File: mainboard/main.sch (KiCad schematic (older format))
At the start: 38 parts, among them Q1 TIP120, U1 LevelShifter

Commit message: first prototype
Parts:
- removed C1: 1uF, Capacitor_THT:CP_Radial_D5.0mm_P2.50mm, symbol Device:CP
- removed CellVoltageOpAmp1: LM358, Package_DIP:DIP-8_W7.62mm_Socket, symbol Amplifier_Operational:LM358
- removed R_Cell1_Vdiv_A1: 33K, Resistor_THT:R_Axial_DIN0207_L6.3mm_D2.5mm_P7.62mm_Horizontal, symbol Device:R
- removed R_Cell1_Vdiv_B1: 100K, Resistor_THT:R_Axial_DIN0207_L6.3mm_D2.5mm_P2.54mm_Vertical, symbol Device:R
- removed R_V_Cell2_1, R_V_Cell2_2, R_V_Cell3_2: 47K, Resistor_THT:R_Axial_DIN0207_L6.3mm_D2.5mm_P2.54mm_Vertical, symbol Device:R
- removed R_V_Cell2_3, R_V_Cell2_4, R_V_Cell3_3, R_V_Cell3_4: 33K, Resistor_THT:R_Axial_DIN0207_L6.3mm_D2.5mm_P2.54mm_Vertical, symbol Device:R
- removed R_V_Cell3_1: 47K, Resistor_THT:R_Axial_DIN0207_L6.3mm_D2.5mm_P5.08mm_Vertical, symbol Device:R
- added Diode2, Diode3: D, Diode_THT:D_T-1_P5.08mm_Horizontal, symbol Device:D
- added RV2: R_POT3Bat, Potentiometer_THT:Potentiometer_Bourns_3296W_Vertical, symbol Device:R_POT_TRIM
- added RV3: R_POT2, Potentiometer_THT:Potentiometer_Bourns_3296W_Vertical, symbol Device:R_POT_TRIM
- added RV4: R_POT1, Potentiometer_THT:Potentiometer_Bourns_3296W_Vertical, symbol Device:R_POT_TRIM
- renumbered Diode1 to Diode1sw1
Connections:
- net PCheck is gone; now on net P_Check: MicroController1.18 (A7)
- net PowerIN is gone; now on net P_IN: MicroController1.17 (D13/SCK)
- net +3V3: no longer Con_Switch1.3 (Pin_3)
- net +BATT: now also RV3.3
- net BATT_Cell_1_2: now also Diode3.2 (A)
- net BATT_Cell_2_3: now also Diode2.2 (A)
- net GND: now also Con_Switch1.3 (Pin_3), RV2.1, RV3.1, RV4.1
- net op2: now also RV2.2
- net op3: now also RV3.2
- net op4: now also RV4.2
- new net: Diode2.1 (K), RV2.3
- new net: Diode3.1 (K), RV4.3

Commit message: again
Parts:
- added R1: ?, Resistor_THT:R_Axial_DIN0207_L6.3mm_D2.5mm_P2.54mm_Vertical, symbol Device:R
- MicroController1: footprint CustomFootprints:Arduino_Pro_Mini_Socket_IZOKEE -> CustomFootprints:Arduino_Pro_Mini_Socket_IZOKEE_no_programming
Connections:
- net at Diode1sw1.1 (K), RV1.3, R_T1.1: now also R1.2; no longer Switch_Connector1.2 (Pin_2)
- new net: R1.1, Switch_Connector1.2 (Pin_2)
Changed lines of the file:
@@
 F 0 "MicroController1" H 2200 2765 50  0000 C CNN
 F 1 "IZOKEEProMini" H 2200 2674 50  0000 C CNN
-F 2 "CustomFootprints:Arduino_Pro_Mini_Socket_IZOKEE" H 2200 800 50  0001 C CNN
+F 2 "CustomFootprints:Arduino_Pro_Mini_Socket_IZOKEE_no_programming" H 2200 800 50  0001 C CNN
 F 3 "" H 2200 800 50  0001 C CNN
 	1    2300 1700
@@
 	-1   0    0    1
 $EndComp
-Connection ~ 5400 1000
 Wire Wire Line
 	5100 1000 5400 1000
-$Comp
-L Transistor_BJT:TIP120 Q1
-U 1 1 5E39FC69
-P 5900 1000
-F 0 "Q1" H 6107 1046 50  0000 L CNN
-F 1 "TIP120" H 6107 955 50  0000 L CNN
-F 2 "Package_TO_SOT_THT:TO-220-3_Vertical" H 6100 925 50  0001 L CIN
-F 3 "http://www.fairchildsemi.com/ds/TI/TIP120.pdf" H 5900 1000 50  0001 L CNN
-	1    5900 1000
-	1    0    0    -1
-$EndComp
 $Comp
 L Device:D Diode1sw1
@@
 F 3 "~" H 5400 850 50  0001 C CNN
 	1    5400 850
-	0    -1   -1   0
-$EndComp
-$Comp
-L Device:R R_T1
-U 1 1 5E3B3275
-P 5550 1000
-F 0 "R_T1" H 5620 1046 50  0000 L CNN
-F 1 "1K" H 5620 955 50  0000 L CNN
-F 2 "Resistor_THT:R_Axial_DIN0207_L6.3mm_D2.5mm_P5.08mm_Vertical" V 5480 1000 50  0001 C CNN
-F 3 "~" H 5550 1000 50  0001 C CNN
-	1    5550 1000
 	0    -1   -1   0
 $EndComp
@@
 Wire Wire Line
 	4300 700  4300 800
-Wire Wire Line
-	4300 900  5100 900
 Wire Wire Line
 	5550 1500 5550 1300
@@
 $EndComp
 $Comp
-L power:GND #PWR?
+L power:GND #PWR0126
 U 1 1 5E5F3BCE
 P 3850 1850
-F 0 "#PWR?" H 3850 1600 50  0001 C CNN
+F 0 "#PWR0126" H 3850 1600 50  0001 C CNN
 F 1 "GND" V 3855 1722 50  0000 R CNN
 F 2 "" H 3850 1850 50  0001 C CNN
@@
 	0    1    -1   0
 $EndComp
+Connection ~ 5400 1000
+$Comp
+L Device:R R_T1
+U 1 1 5E3B3275
+P 5550 1000
+F 0 "R_T1" H 5620 1046 50  0000 L CNN
+F 1 "1K" H 5620 955 50  0000 L CNN
+F 2 "Resistor_THT:R_Axial_DIN0207_L6.3mm_D2.5mm_P5.08mm_Vertical" V 5480 1000 50  0001 C CNN
+F 3 "~" H 5550 1000 50  0001 C CNN
+	1    5550 1000
+	0    -1   -1   0
+$EndComp
+$Comp
+L Transistor_BJT:TIP120 Q1
+U 1 1 5E39FC69
+P 5900 1000
+F 0 "Q1" H 6107 1046 50  0000 L CNN
+F 1 "TIP120" H 6107 955 50  0000 L CNN
+F 2 "Package_TO_SOT_THT:TO-220-3_Vertical" H 6100 925 50  0001 L CIN
+F 3 "http://www.fairchildsemi.com/ds/TI/TIP120.pdf" H 5900 1000 50  0001 L CNN
+	1    5900 1000
+	1    0    0    -1
+$EndComp
+$Comp
+L Device:R R1
+U 1 1 5E5F87D4
+P 4800 900
+F 0 "R1" H 4870 946 50  0000 L CNN
+F 1 "?" H 4870 855 50  0000 L CNN
+F 2 "Resistor_THT:R_Axial_DIN0207_L6.3mm_D2.5mm_P2.54mm_Vertical" V 4730 900 50  0001 C CNN
+F 3 "~" H 4800 900 50  0001 C CNN
+	1    4800 900
+	0    -1   -1   0
+$EndComp
+Wire Wire Line
+	4950 900  5100 900
+Wire Wire Line
+	4650 900  4300 900
 $EndSCHEMATC

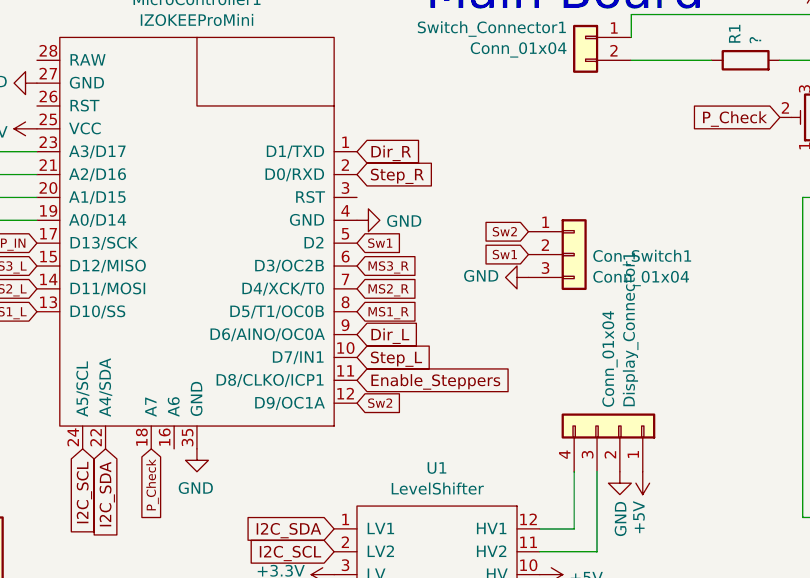
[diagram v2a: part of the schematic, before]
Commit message: pwm pins
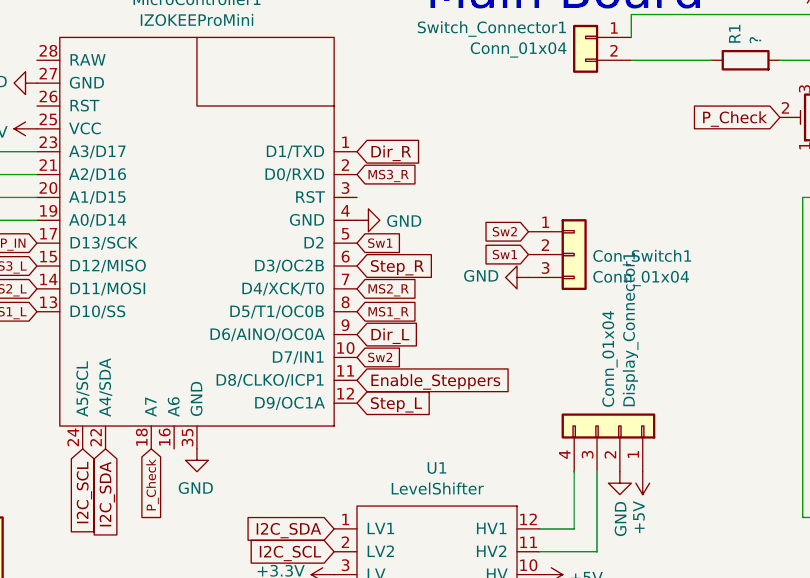
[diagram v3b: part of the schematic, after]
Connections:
- net MS3_R: now also MicroController1.2 (D0/RXD); no longer MicroController1.6 (D3/OC2B)
- net Step_L: now also MicroController1.12 (D9/OC1A); no longer MicroController1.10 (D7/IN1)
- net Step_R: now also MicroController1.6 (D3/OC2B); no longer MicroController1.2 (D0/RXD)
- net Sw2: now also MicroController1.10 (D7/IN1); no longer MicroController1.12 (D9/OC1A)
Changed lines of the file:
@@
 	1    0    0    -1
 $EndComp
-Text GLabel 3100 1800 2    40   Input ~ 0
+Text GLabel 3100 1400 2    40   Input ~ 0
 MS3_R
 Text GLabel 3100 1900 2    40   Input ~ 0
@@
 Text GLabel 3100 1300 2    50   Input ~ 0
 Dir_R
-Text GLabel 3100 1400 2    50   Input ~ 0
+Text GLabel 3100 1800 2    50   Input ~ 0
 Step_R
 Text GLabel 3100 2100 2    50   Input ~ 0
 Dir_L
-Text GLabel 3100 2200 2    50   Input ~ 0
+Text GLabel 3100 2400 2    50   Input ~ 0
 Step_L
 Text GLabel 1800 6550 0    50   Input ~ 0
@@
 Text GLabel 3100 1700 2    40   Input ~ 0
 Sw1
-Text GLabel 3100 2400 2    40   Input ~ 0
+Text GLabel 3100 2200 2    40   Input ~ 0
 Sw2
 Text GLabel 3850 1750 0    40   Input ~ 0

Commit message: larger capacitor footprints
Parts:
- C2, C_MD_L1, C_MD_L2: footprint Capacitor_THT:CP_Radial_D5.0mm_P2.50mm -> Capacitor_THT:CP_Radial_D6.3mm_P2.50mm
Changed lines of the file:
@@
 F 0 "C_MD_L2" H 1168 7146 50  0000 L CNN
 F 1 "100uF" H 1168 7055 50  0000 L CNN
-F 2 "Capacitor_THT:CP_Radial_D5.0mm_P2.50mm" H 1088 6950 50  0001 C CNN
+F 2 "Capacitor_THT:CP_Radial_D6.3mm_P2.50mm" H 1088 6950 50  0001 C CNN
 F 3 "~" H 1050 7100 50  0001 C CNN
 	1    1050 7100
@@
 F 0 "C_MD_L1" H 1118 4896 50  0000 L CNN
 F 1 "100uF" H 1118 4805 50  0000 L CNN
-F 2 "Capacitor_THT:CP_Radial_D5.0mm_P2.50mm" H 1038 4700 50  0001 C CNN
+F 2 "Capacitor_THT:CP_Radial_D6.3mm_P2.50mm" H 1038 4700 50  0001 C CNN
 F 3 "~" H 1000 4850 50  0001 C CNN
 	1    1000 4850
@@
 F 0 "C2" H 10068 2246 50  0000 L CNN
 F 1 "1uF" H 10068 2155 50  0000 L CNN
-F 2 "Capacitor_THT:CP_Radial_D5.0mm_P2.50mm" H 9988 2050 50  0001 C CNN
+F 2 "Capacitor_THT:CP_Radial_D6.3mm_P2.50mm" H 9988 2050 50  0001 C CNN
 F 3 "~" H 9950 2200 50  0001 C CNN
 	1    9950 2200

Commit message: Mainboard changes
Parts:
- C2, C_MD_L1, C_MD_L2: footprint Capacitor_THT:CP_Radial_D6.3mm_P2.50mm -> Capacitor_THT:CP_Radial_D5.0mm_P2.50mm
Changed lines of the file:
@@
 F 0 "C_MD_L2" H 1168 7146 50  0000 L CNN
 F 1 "100uF" H 1168 7055 50  0000 L CNN
-F 2 "Capacitor_THT:CP_Radial_D6.3mm_P2.50mm" H 1088 6950 50  0001 C CNN
+F 2 "Capacitor_THT:CP_Radial_D5.0mm_P2.50mm" H 1088 6950 50  0001 C CNN
 F 3 "~" H 1050 7100 50  0001 C CNN
 	1    1050 7100
@@
 F 0 "C_MD_L1" H 1118 4896 50  0000 L CNN
 F 1 "100uF" H 1118 4805 50  0000 L CNN
-F 2 "Capacitor_THT:CP_Radial_D6.3mm_P2.50mm" H 1038 4700 50  0001 C CNN
+F 2 "Capacitor_THT:CP_Radial_D5.0mm_P2.50mm" H 1038 4700 50  0001 C CNN
 F 3 "~" H 1000 4850 50  0001 C CNN
 	1    1000 4850
@@
 F 0 "C2" H 10068 2246 50  0000 L CNN
 F 1 "1uF" H 10068 2155 50  0000 L CNN
-F 2 "Capacitor_THT:CP_Radial_D6.3mm_P2.50mm" H 9988 2050 50  0001 C CNN
+F 2 "Capacitor_THT:CP_Radial_D5.0mm_P2.50mm" H 9988 2050 50  0001 C CNN
 F 3 "~" H 9950 2200 50  0001 C CNN
 	1    9950 2200

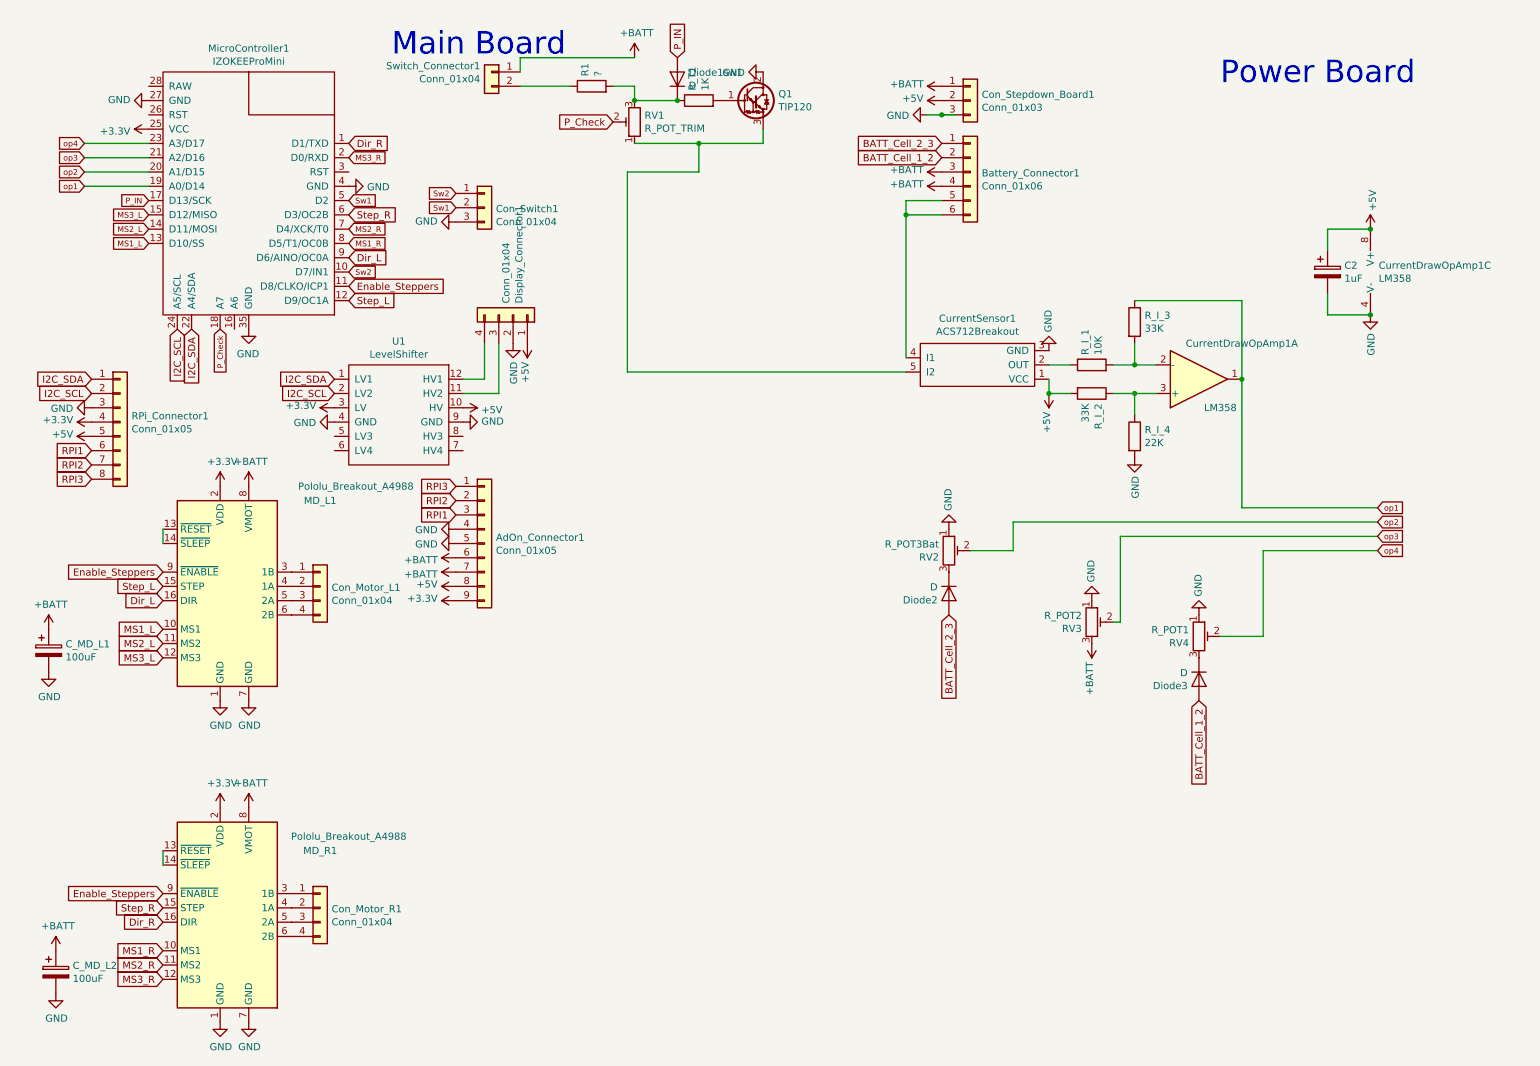
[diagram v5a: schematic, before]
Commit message: Major re-layouting and cleanup
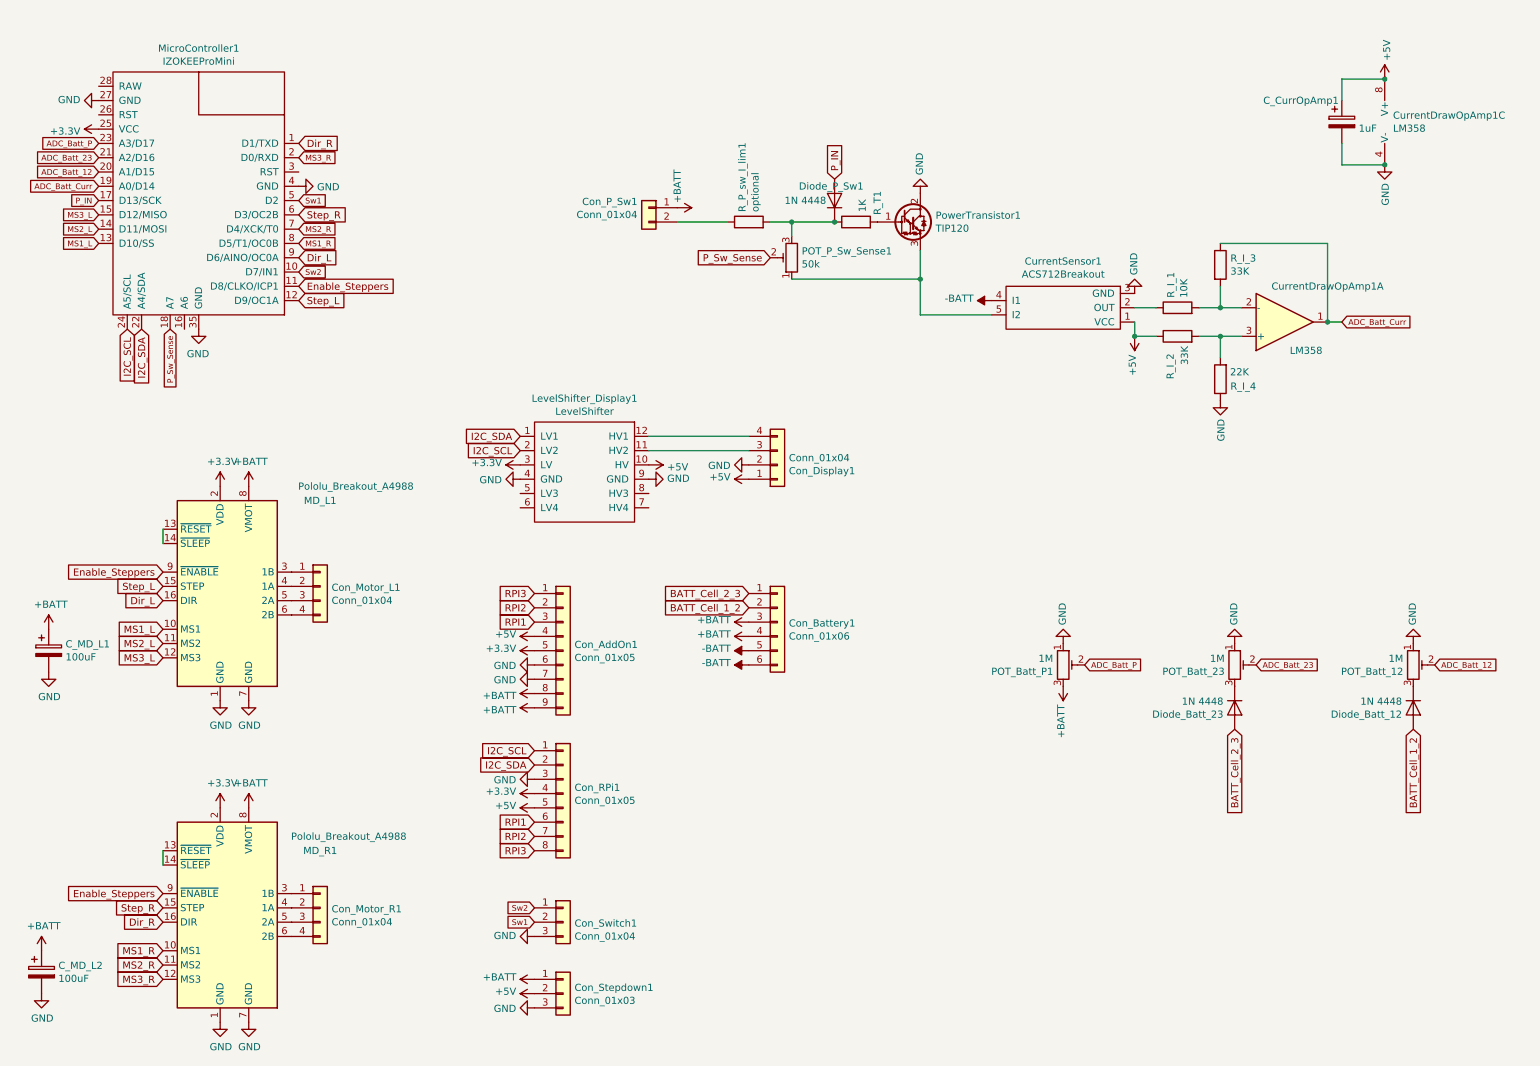
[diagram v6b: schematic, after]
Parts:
- Diode_Batt_12: renamed from Diode3; value D -> 1N 4448
- Diode_Batt_23: renamed from Diode2; value D -> 1N 4448
- Diode_P_Sw1: renamed from Diode1sw1; value D -> 1N 4448; footprint Diode_THT:D_T-1_P5.08mm_Horizontal -> Diode_THT:D_T-1_P10.16mm_Horizontal
- MicroController1: footprint CustomFootprints:Arduino_Pro_Mini_Socket_IZOKEE_no_programming -> CustomFootprints:Arduino_Pro_Mini_Socket_IZOKEE_no_programming_no_ext_wire
- POT_Batt_12: renamed from RV4; value R_POT1 -> 1M
- POT_Batt_23: renamed from RV2; value R_POT3Bat -> 1M
- POT_Batt_P1: renamed from RV3; value R_POT2 -> 1M
- POT_P_Sw_Sense1: renamed from RV1; value R_POT_TRIM -> 50k
- R_I_1: footprint Resistor_THT:R_Axial_DIN0207_L6.3mm_D2.5mm_P5.08mm_Vertical -> Resistor_THT:R_Axial_DIN0207_L6.3mm_D2.5mm_P7.62mm_Horizontal
- R_P_sw_I_lim1: renamed from R1; value ? -> optional
- R_T1: footprint Resistor_THT:R_Axial_DIN0207_L6.3mm_D2.5mm_P5.08mm_Vertical -> Resistor_THT:R_Axial_DIN0207_L6.3mm_D2.5mm_P2.54mm_Vertical
- renumbered C2 to C_CurrOpAmp1, AdOn_Connector1 to Con_AddOn1, Battery_Connector1 to Con_Battery1, Display_Connector1 to Con_Display1, Switch_Connector1 to Con_P_Sw1, RPi_Connector1 to Con_RPi1, Con_Stepdown_Board1 to Con_Stepdown1, U1 to LevelShifter_Display1, Q1 to PowerTransistor1
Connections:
- net +3V3: now also Con_AddOn1.5 (Pin_5); no longer Con_AddOn1.9 (Pin_9)
- net +5V: now also Con_AddOn1.4 (Pin_4), R_I_2.1; no longer Con_AddOn1.8 (Pin_8), R_I_2.2
- net +BATT: now also Con_AddOn1.8 (Pin_8), Con_AddOn1.9 (Pin_9); no longer Con_AddOn1.6 (Pin_6), Con_AddOn1.7 (Pin_7)
- net GND: now also Con_AddOn1.6 (Pin_6), Con_AddOn1.7 (Pin_7), R_I_4.1; no longer Con_AddOn1.4 (Pin_4), Con_AddOn1.5 (Pin_5), R_I_4.2
- net I2C_SCL: now also Con_RPi1.1 (Pin_1); no longer Con_RPi1.2 (Pin_2)
- net I2C_SDA: now also Con_RPi1.2 (Pin_2); no longer Con_RPi1.1 (Pin_1)
- net -BATT: now reaches Con_Battery1.5 (Pin_5), Con_Battery1.6 (Pin_6), CurrentSensor1.4 (I1)
- net P_Check renamed P_Sw_Sense
- net op1 renamed ADC_Batt_Curr
- net op2 renamed ADC_Batt_12
- net ADC_Batt_12: now also POT_Batt_12.2; no longer POT_Batt_23.2
- net op3 renamed ADC_Batt_23
- net ADC_Batt_23: now also POT_Batt_23.2; no longer POT_Batt_P1.2
- net op4 renamed ADC_Batt_P
- net ADC_Batt_P: now also POT_Batt_P1.2; no longer POT_Batt_12.2
- new net: CurrentDrawOpAmp1.3 (+), R_I_2.2, R_I_4.2
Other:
- note removed: "Main Board"
- note removed: "Power Board"
- moved on the sheet: C_CurrOpAmp1, C_MD_L2, Con_AddOn1, Con_Battery1, Con_Display1, Con_P_Sw1, Con_RPi1, Con_Stepdown1, Con_Switch1, CurrentDrawOpAmp1A, CurrentDrawOpAmp1C, CurrentSensor1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

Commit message: Minor polishing for submission
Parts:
- renumbered C_MD_L2 to C_MD_R1
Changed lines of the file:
@@
 MS1_R
 $Comp
-L Device:CP C_MD_L2
+L Device:CP C_MD_R1
 U 1 1 5D878D95
 P 950 7100
-F 0 "C_MD_L2" H 1068 7146 50  0000 L CNN
+F 0 "C_MD_R1" H 1068 7146 50  0000 L CNN
 F 1 "100uF" H 1068 7055 50  0000 L CNN
 F 2 "Capacitor_THT:CP_Radial_D5.0mm_P2.50mm" H 988 6950 50  0001 C CNN

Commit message: Various smaller fixes
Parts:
- Con_AddOn1: value Conn_01x05 -> Conn_01x09
- Con_P_Sw1: value Conn_01x04 -> Conn_01x02
- Con_RPi1: value Conn_01x05 -> Conn_01x08
- Con_Switch1: value Conn_01x04 -> Conn_01x03
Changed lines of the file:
@@
 P 4600 5850
 F 0 "Con_RPi1" H 4680 5892 50  0000 L CNN
-F 1 "Conn_01x05" H 4680 5801 50  0000 L CNN
+F 1 "Conn_01x08" H 4680 5801 50  0000 L CNN
 F 2 "Connector_JST:JST_XH_B8B-XH-A_1x08_P2.50mm_Vertical" H 4600 5850 50  0001 C CNN
 F 3 "~" H 4600 5850 50  0001 C CNN
@@
 P 4600 4850
 F 0 "Con_AddOn1" H 4680 4892 50  0000 L CNN
-F 1 "Conn_01x05" H 4680 4801 50  0000 L CNN
+F 1 "Conn_01x09" H 4680 4801 50  0000 L CNN
 F 2 "Connector_JST:JST_XH_B9B-XH-A_1x09_P2.50mm_Vertical" H 4600 4850 50  0001 C CNN
 F 3 "~" H 4600 4850 50  0001 C CNN
@@
 P 4600 6750
 F 0 "Con_Switch1" H 4680 6742 50  0000 L CNN
-F 1 "Conn_01x04" H 4680 6651 50  0000 L CNN
+F 1 "Conn_01x03" H 4680 6651 50  0000 L CNN
 F 2 "Connector_JST:JST_XH_B3B-XH-A_1x03_P2.50mm_Vertical" H 4600 6750 50  0001 C CNN
 F 3 "~" H 4600 6750 50  0001 C CNN
@@
 P 5200 1750
 F 0 "Con_P_Sw1" H 5280 1792 50  0000 L CNN
-F 1 "Conn_01x04" H 5280 1701 50  0000 L CNN
+F 1 "Conn_01x02" H 5280 1701 50  0000 L CNN
 F 2 "Connector_JST:JST_XH_B2B-XH-A_1x02_P2.50mm_Vertical" H 5200 1750 50  0001 C CNN
 F 3 "~" H 5200 1750 50  0001 C CNN
